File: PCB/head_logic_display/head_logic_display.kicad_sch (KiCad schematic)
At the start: 71 parts, among them J1 Conn_01x03_Socket, J2 Conn_01x03_Socket

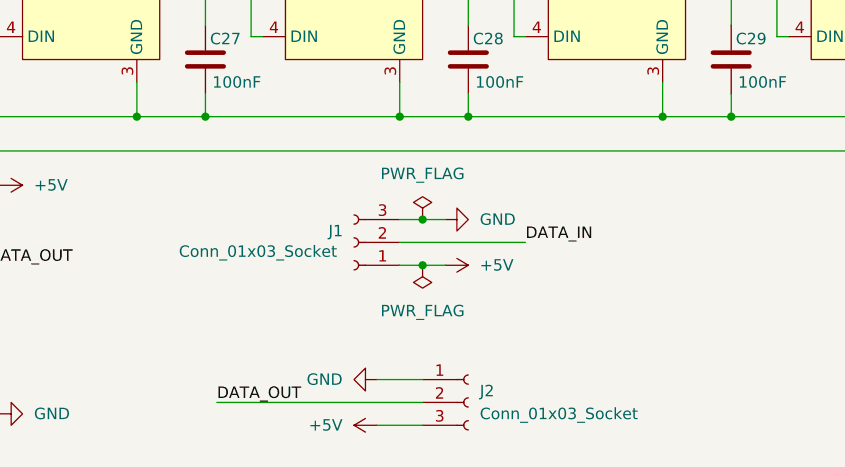
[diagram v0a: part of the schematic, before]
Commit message: Finish component placement
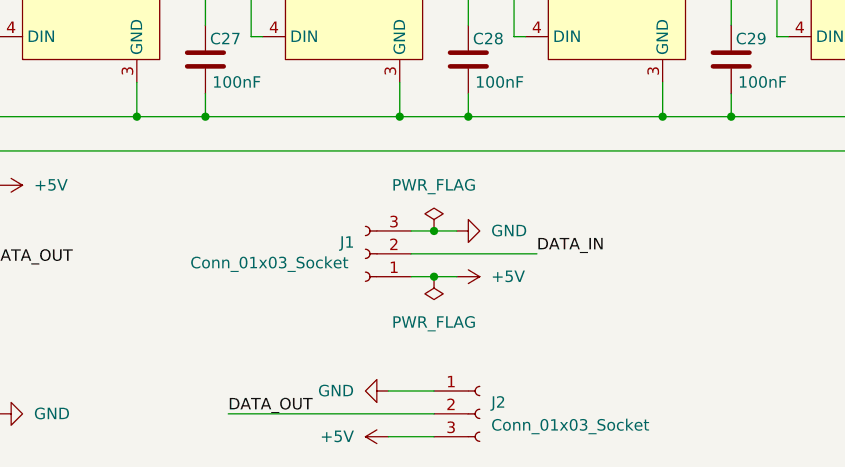
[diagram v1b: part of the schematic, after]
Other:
- moved on the sheet: J1, J2
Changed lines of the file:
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@@
 	)
 	(junction
-		(at 140.97 157.48)
+		(at 142.24 158.75)
 		(diameter 0)
 		(color 0 0 0 0)
@@
 	)
 	(junction
-		(at 140.97 152.4)
+		(at 142.24 153.67)
 		(diameter 0)
 		(color 0 0 0 0)
@@
 	(wire
 		(pts
-			(xy 140.97 157.48) (xy 143.51 157.48)
+			(xy 142.24 158.75) (xy 144.78 158.75)
 		)
 		(stroke
@@
 	(wire
 		(pts
-			(xy 138.43 154.94) (xy 152.4 154.94)
+			(xy 139.7 156.21) (xy 153.67 156.21)
 		)
 		(stroke
@@
 	(wire
 		(pts
-			(xy 135.89 170.18) (xy 140.97 170.18)
+			(xy 137.16 171.45) (xy 142.24 171.45)
 		)
 		(stroke
@@
 	(wire
 		(pts
-			(xy 118.11 172.72) (xy 140.97 172.72)
+			(xy 119.38 173.99) (xy 142.24 173.99)
 		)
 		(stroke
@@
 	(wire
 		(pts
-			(xy 138.43 157.48) (xy 140.97 157.48)
+			(xy 139.7 158.75) (xy 142.24 158.75)
 		)
 		(stroke
@@
 	(wire
 		(pts
-			(xy 138.43 152.4) (xy 140.97 152.4)
+			(xy 139.7 153.67) (xy 142.24 153.67)
 		)
 		(stroke
@@
 	(wire
 		(pts
-			(xy 140.97 152.4) (xy 143.51 152.4)
+			(xy 142.24 153.67) (xy 144.78 153.67)
 		)
 		(stroke
@@
 	(wire
 		(pts
-			(xy 135.89 175.26) (xy 140.97 175.26)
+			(xy 137.16 176.53) (xy 142.24 176.53)
 		)
 		(stroke
@@
 	)
 	(label "DATA_IN"
-		(at 152.4 154.94 0)
+		(at 153.67 156.21 0)
 		(fields_autoplaced yes)
 		(effects
@@
 	)
 	(label "DATA_OUT"
-		(at 118.11 172.72 0)
+		(at 119.38 173.99 0)
 		(fields_autoplaced yes)
 		(effects
@@
 	(symbol
 		(lib_id "power:PWR_FLAG")
-		(at 140.97 152.4 0)
+		(at 142.24 153.67 0)
 		(unit 1)
 		(exclude_from_sim no)
@@
 		(fields_autoplaced yes)
 		(property "Reference" "#FLG01"
-			(at 140.97 150.495 0)
+			(at 142.24 151.765 0)
 			(effects
 				(font
@@
 		)
 		(property "Value" "PWR_FLAG"
-			(at 140.97 147.32 0)
+			(at 142.24 148.59 0)
 			(effects
 				(font
@@
 		)
 		(property "Footprint" ""
-			(at 140.97 152.4 0)
+			(at 142.24 153.67 0)
 			(effects
 				(font
@@
 		)
 		(property "Datasheet" "~"
-			(at 140.97 152.4 0)
+			(at 142.24 153.67 0)
 			(effects
 				(font
@@
 		)
 		(property "Description" "Special symbol for telling ERC where power comes from"
-			(at 140.97 152.4 0)
+			(at 142.24 153.67 0)
 			(effects
 				(font
@@
 	(symbol
 		(lib_id "power:PWR_FLAG")
-		(at 140.97 157.48 180)
+		(at 142.24 158.75 180)
 		(unit 1)
 		(exclude_from_sim no)
@@
 		(fields_autoplaced yes)
 		(property "Reference" "#FLG02"
-			(at 140.97 159.385 0)
+			(at 142.24 160.655 0)
 			(effects
 				(font
@@
 		)
 		(property "Value" "PWR_FLAG"
-			(at 140.97 162.56 0)
+			(at 142.24 163.83 0)
 			(effects
 				(font
@@
 		)
 		(property "Footprint" ""
-			(at 140.97 157.48 0)
+			(at 142.24 158.75 0)
 			(effects
 				(font
@@
 		)
 		(property "Datasheet" "~"
-			(at 140.97 157.48 0)
+			(at 142.24 158.75 0)
 			(effects
 				(font
@@
 		)
 		(property "Description" "Special symbol for telling ERC where power comes from"
-			(at 140.97 157.48 0)
+			(at 142.24 158.75 0)
 			(effects
 				(font
@@
 	(symbol
 		(lib_id "Connector:Conn_01x03_Socket")
-		(at 133.35 154.94 180)
+		(at 134.62 156.21 180)
 		(unit 1)
 		(exclude_from_sim no)
@@
 		(dnp no)
 		(property "Reference" "J1"
-			(at 131.318 153.67 0)
+			(at 132.588 154.94 0)
 			(effects
 				(font
@@
 		)
 		(property "Value" "Conn_01x03_Socket"
-			(at 122.682 155.956 0)
+			(at 123.952 157.226 0)
 			(effects
 				(font
@@
 		)
 		(property "Footprint" "Connector_JST:JST_XH_S3B-XH-A-1_1x03_P2.50mm_Horizontal"
-			(at 133.35 154.94 0)
+			(at 134.62 156.21 0)
 			(effects
 				(font
@@
 		)
 		(property "Datasheet" "~"
-			(at 133.35 154.94 0)
+			(at 134.62 156.21 0)
 			(effects
 				(font
@@
 		)
 		(property "Description" "Generic connector, single row, 01x03, script generated"
-			(at 133.35 154.94 0)
+			(at 134.62 156.21 0)
 			(effects
 				(font
@@
 	(symbol
 		(lib_id "power:GND")
-		(at 135.89 170.18 270)
+		(at 137.16 171.45 270)
 		(unit 1)
 		(exclude_from_sim no)
@@
 		(fields_autoplaced yes)
 		(property "Reference" "#PWR024"
-			(at 129.54 170.18 0)
+			(at 130.81 171.45 0)
 			(effects
 				(font
@@
 		)
 		(property "Value" "GND"
-			(at 132.08 170.1799 90)
+			(at 133.35 171.4499 90)
 			(effects
 				(font
@@
 		)
 		(property "Footprint" ""
-			(at 135.89 170.18 0)
+			(at 137.16 171.45 0)
 			(effects
 				(font
@@
 		)
 		(property "Datasheet" ""
-			(at 135.89 170.18 0)
+			(at 137.16 171.45 0)
 			(effects
 				(font
@@
 		)
 		(property "Description" "Power symbol creates a global label with name \"GND\" , ground"
-			(at 135.89 170.18 0)
+			(at 137.16 171.45 0)
 			(effects
 				(font
@@
 	(symbol
 		(lib_id "Connector:Conn_01x03_Socket")
-		(at 146.05 172.72 0)
+		(at 147.32 173.99 0)
 		(unit 1)
 		(exclude_from_sim no)
@@
 		(fields_autoplaced yes)
 		(property "Reference" "J2"
-			(at 147.32 171.4499 0)
+			(at 148.59 172.7199 0)
 			(effects
 				(font
@@
 		)
 		(property "Value" "Conn_01x03_Socket"
-			(at 147.32 173.9899 0)
+			(at 148.59 175.2599 0)
 			(effects
 				(font
@@
 		)
 		(property "Footprint" "Connector_JST:JST_XH_S3B-XH-A-1_1x03_P2.50mm_Horizontal"
-			(at 146.05 172.72 0)
+			(at 147.32 173.99 0)
 			(effects
 				(font
@@
 		)
 		(property "Datasheet" "~"
-			(at 146.05 172.72 0)
+			(at 147.32 173.99 0)
 			(effects
 				(font
@@
 		)
 		(property "Description" "Generic connector, single row, 01x03, script generated"
-			(at 146.05 172.72 0)
+			(at 147.32 173.99 0)
 			(effects
 				(font
@@
 	(symbol
 		(lib_id "power:+5V")
-		(at 135.89 175.26 90)
+		(at 137.16 176.53 90)
 		(unit 1)
 		(exclude_from_sim no)
@@
 		(fields_autoplaced yes)
 		(property "Reference" "#PWR023"
-			(at 139.7 175.26 0)
+			(at 140.97 176.53 0)
 			(effects
 				(font
@@
 		)
 		(property "Value" "+5V"
-			(at 132.08 175.2599 90)
+			(at 133.35 176.5299 90)
 			(effects
 				(font
@@
 		)
 		(property "Footprint" ""
-			(at 135.89 175.26 0)
+			(at 137.16 176.53 0)
 			(effects
 				(font
@@
 		)
 		(property "Datasheet" ""
-			(at 135.89 175.26 0)
+			(at 137.16 176.53 0)
 			(effects
 				(font
@@
 		)
 		(property "Description" "Power symbol creates a global label with name \"+5V\""
-			(at 135.89 175.26 0)
+			(at 137.16 176.53 0)
 			(effects
 				(font
@@
 	(symbol
 		(lib_id "power:GND")
-		(at 143.51 152.4 90)
+		(at 144.78 153.67 90)
 		(unit 1)
 		(exclude_from_sim no)
@@
 		(fields_autoplaced yes)
 		(property "Reference" "#PWR021"
-			(at 149.86 152.4 0)
+			(at 151.13 153.67 0)
 			(effects
 				(font
@@
 		)
 		(property "Value" "GND"
-			(at 147.32 152.3999 90)
+			(at 148.59 153.6699 90)
 			(effects
 				(font
@@
 		)
 		(property "Footprint" ""
-			(at 143.51 152.4 0)
+			(at 144.78 153.67 0)
 			(effects
 				(font
@@
 		)
 		(property "Datasheet" ""
-			(at 143.51 152.4 0)
+			(at 144.78 153.67 0)
 			(effects
 				(font
@@
 		)
 		(property "Description" "Power symbol creates a global label with name \"GND\" , ground"
-			(at 143.51 152.4 0)
+			(at 144.78 153.67 0)
 			(effects
 				(font
@@
 	(symbol
 		(lib_id "power:+5V")
-		(at 143.51 157.48 270)
+		(at 144.78 158.75 270)
 		(unit 1)
 		(exclude_from_sim no)
@@
 		(fields_autoplaced yes)
 		(property "Reference" "#PWR022"
-			(at 139.7 157.48 0)
+			(at 140.97 158.75 0)
 			(effects
 				(font
@@
 		)
 		(property "Value" "+5V"
-			(at 147.32 157.4799 90)
+			(at 148.59 158.7499 90)
 			(effects
 				(font
@@
 		)
 		(property "Footprint" ""
-			(at 143.51 157.48 0)
+			(at 144.78 158.75 0)
 			(effects
 				(font
@@
 		)
 		(property "Datasheet" ""
-			(at 143.51 157.48 0)
+			(at 144.78 158.75 0)
 			(effects
 				(font
@@
 		)
 		(property "Description" "Power symbol creates a global label with name \"+5V\""
-			(at 143.51 157.48 0)
+			(at 144.78 158.75 0)
 			(effects
 				(font

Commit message: Finish board layout
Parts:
- added H1, H2: MountingHole_Pad, MountingHole:MountingHole_2.5mm_Pad_Via, symbol Mechanical:MountingHole_Pad
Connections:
- net GND: now also H1.1, H2.1

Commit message: Rev 1.0 boards ordered
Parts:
- J1, J2: now left out of the parts list
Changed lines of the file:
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@@
 	)
 	(symbol
+		(lib_name "Conn_01x03_Socket_1")
 		(lib_id "Connector:Conn_01x03_Socket")
 		(at 134.62 156.21 180)
 		(unit 1)
 		(exclude_from_sim no)
-		(in_bom yes)
+		(in_bom no)
 		(on_board yes)
 		(dnp no)
@@
 		(unit 1)
 		(exclude_from_sim no)
-		(in_bom yes)
+		(in_bom no)
 		(on_board yes)
 		(dnp no)
